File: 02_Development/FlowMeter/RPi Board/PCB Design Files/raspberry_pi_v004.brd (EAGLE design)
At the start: 111.8 x 128.3 mm, 120 parts, among them J5 POWER_JACK, P1 SPL006-007, P2 SPL006-007, P3 SPL006-007, P4 SPL006-007, P5 SPL006-007, Q1 4.3A/20V/54mΩ, Q2 500mA/300V, U6 TCA9548APWR, U7 TCA9548APWR

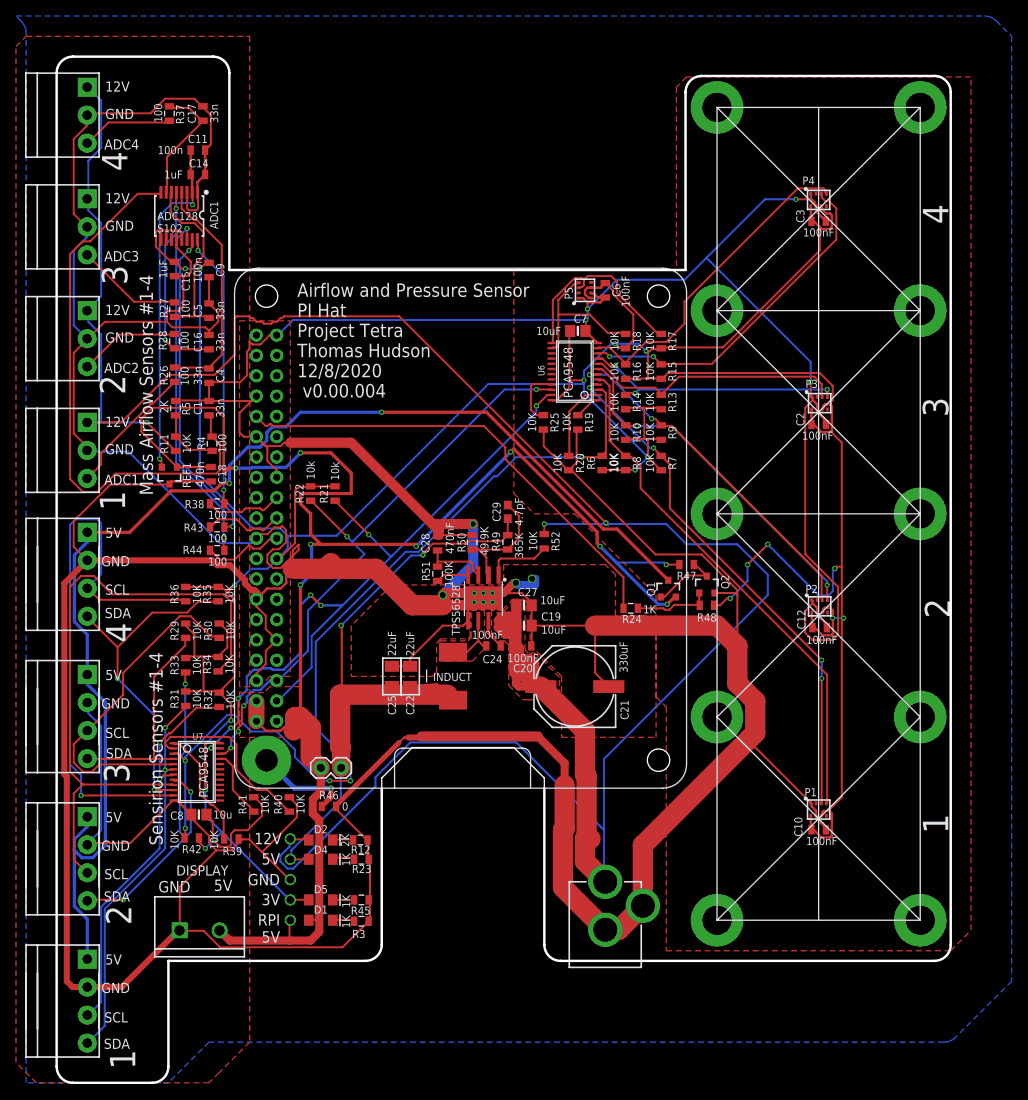
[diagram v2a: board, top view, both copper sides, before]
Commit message: Next revision of PCB
Changed I2C pullup resistors to 3Kohm

General tidy up and fix of issues on the PCB. Tweaked some polygons to eliminate sharp corners, made some traces larger.
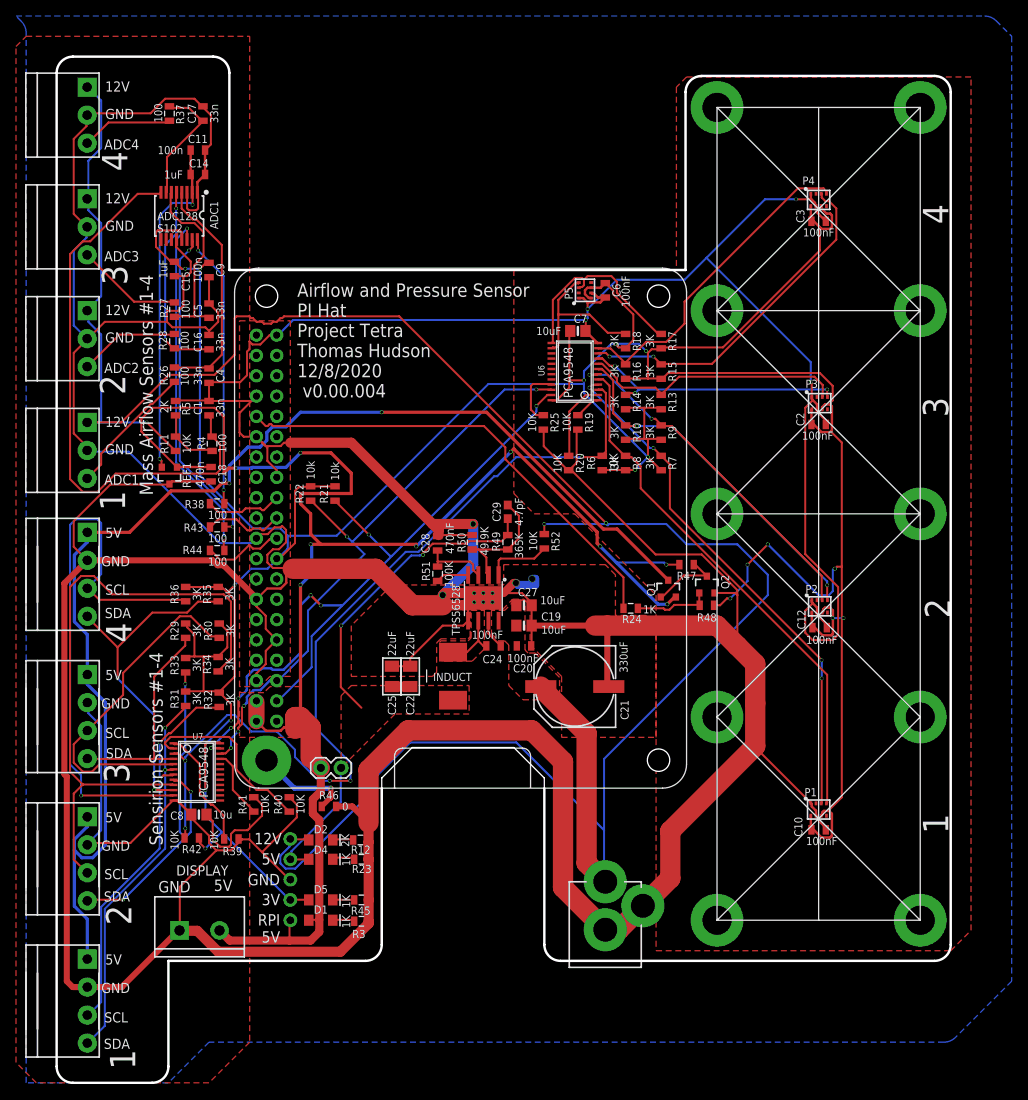
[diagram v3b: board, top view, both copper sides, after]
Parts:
- R10, R13, R14, R15, R16, R17, R18, R29, R30, R31, R32, R33, R34, R35, R36, R7, R8, R9: value 10K -> 3K
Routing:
- net 12V: track 355.7 -> 307.9 mm
- net 5V: track 85.1 -> 57.8 mm
- net GND: track 948.0 -> 948.9 mm
- added copper zone on layer 1, net 5V

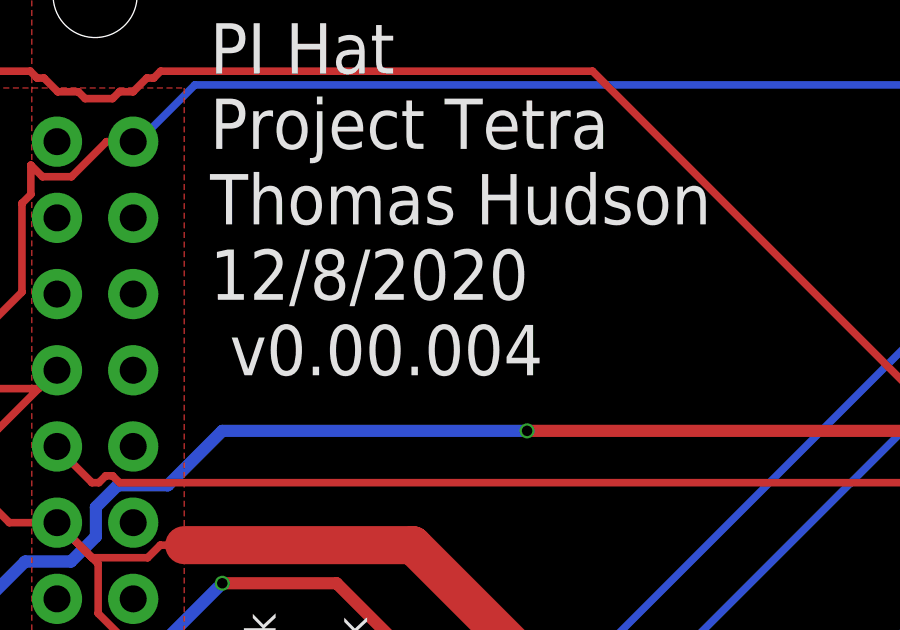
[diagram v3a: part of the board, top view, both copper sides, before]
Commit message: Changes made as per PR152
Changes made as requested, I also updated the pdf of the schematic and the dru file.

One thing I have noticed is that generating the BOM automatically comes up with the incorrect resistor value of 0.3 Ohms. I suspect this is to do with the library that is being used.
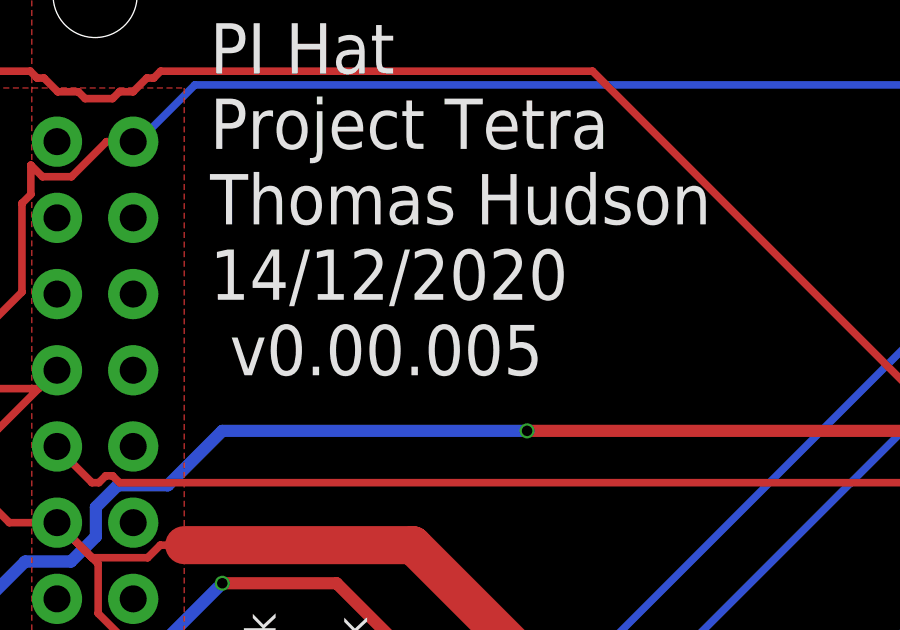
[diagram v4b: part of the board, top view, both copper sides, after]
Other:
- board text added: "Airflow and Pressure Sensor PI Hat Project Tetra Thomas Hudson 14/12/2020 v0.00.005"
- board text removed: "Airflow and Pressure Sensor PI Hat Project Tetra Thomas Hudson 12/8/2020 v0.00.004"
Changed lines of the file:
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@@
 Project Tetra
 Thomas Hudson
-12/8/2020
- v0.00.004</text>
+14/12/2020
+ v0.00.005</text>
 <text x="-17.2212" y="-17.2974" size="1.6764" layer="21" ratio="15" rot="R90" align="bottom-right">Sensirion Sensors #1-4</text>
 <text x="-25.0952" y="2.8956" size="3.175" layer="21" ratio="15" rot="R270">1</text>
